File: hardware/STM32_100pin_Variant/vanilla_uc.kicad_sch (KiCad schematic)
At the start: 22 parts, among them J4 , U4 STM32L4S7VITx, U5 ATA6561-GAQW-N, Y2 Crystal_GND24

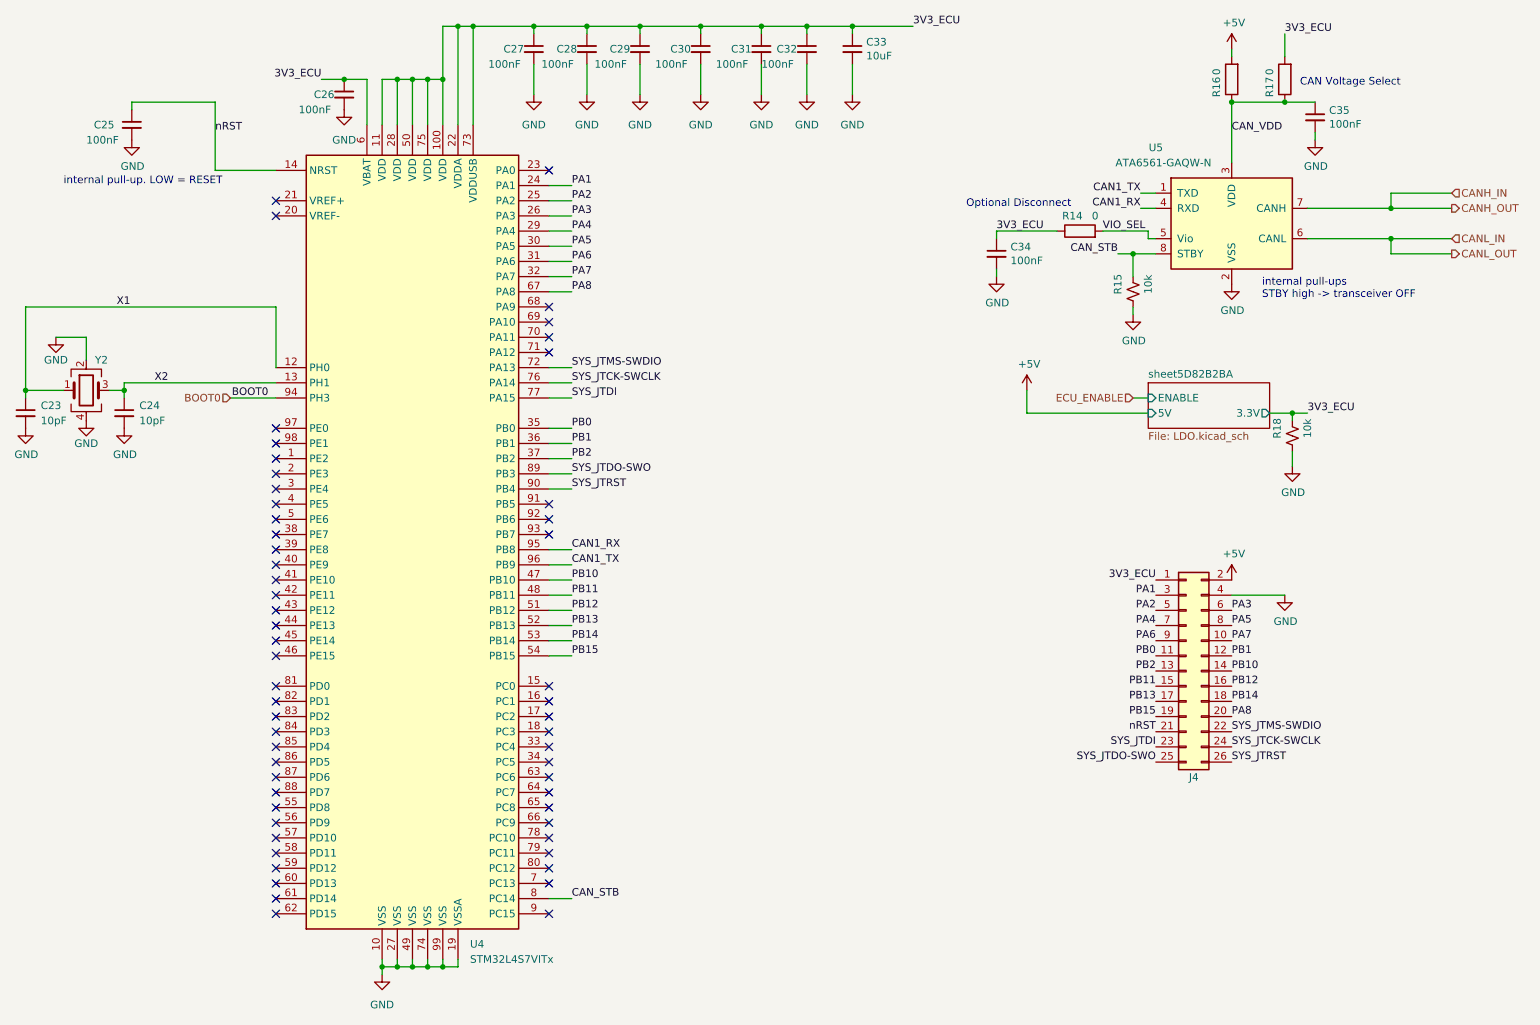
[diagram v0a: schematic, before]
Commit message: Schematic wiring fix, added part numbers
- Fixed missing connections between VREF+ and VDDA, VREF- and VSSA on all ECUs

- Added component part numbers for crystal and CAN trx to schematic
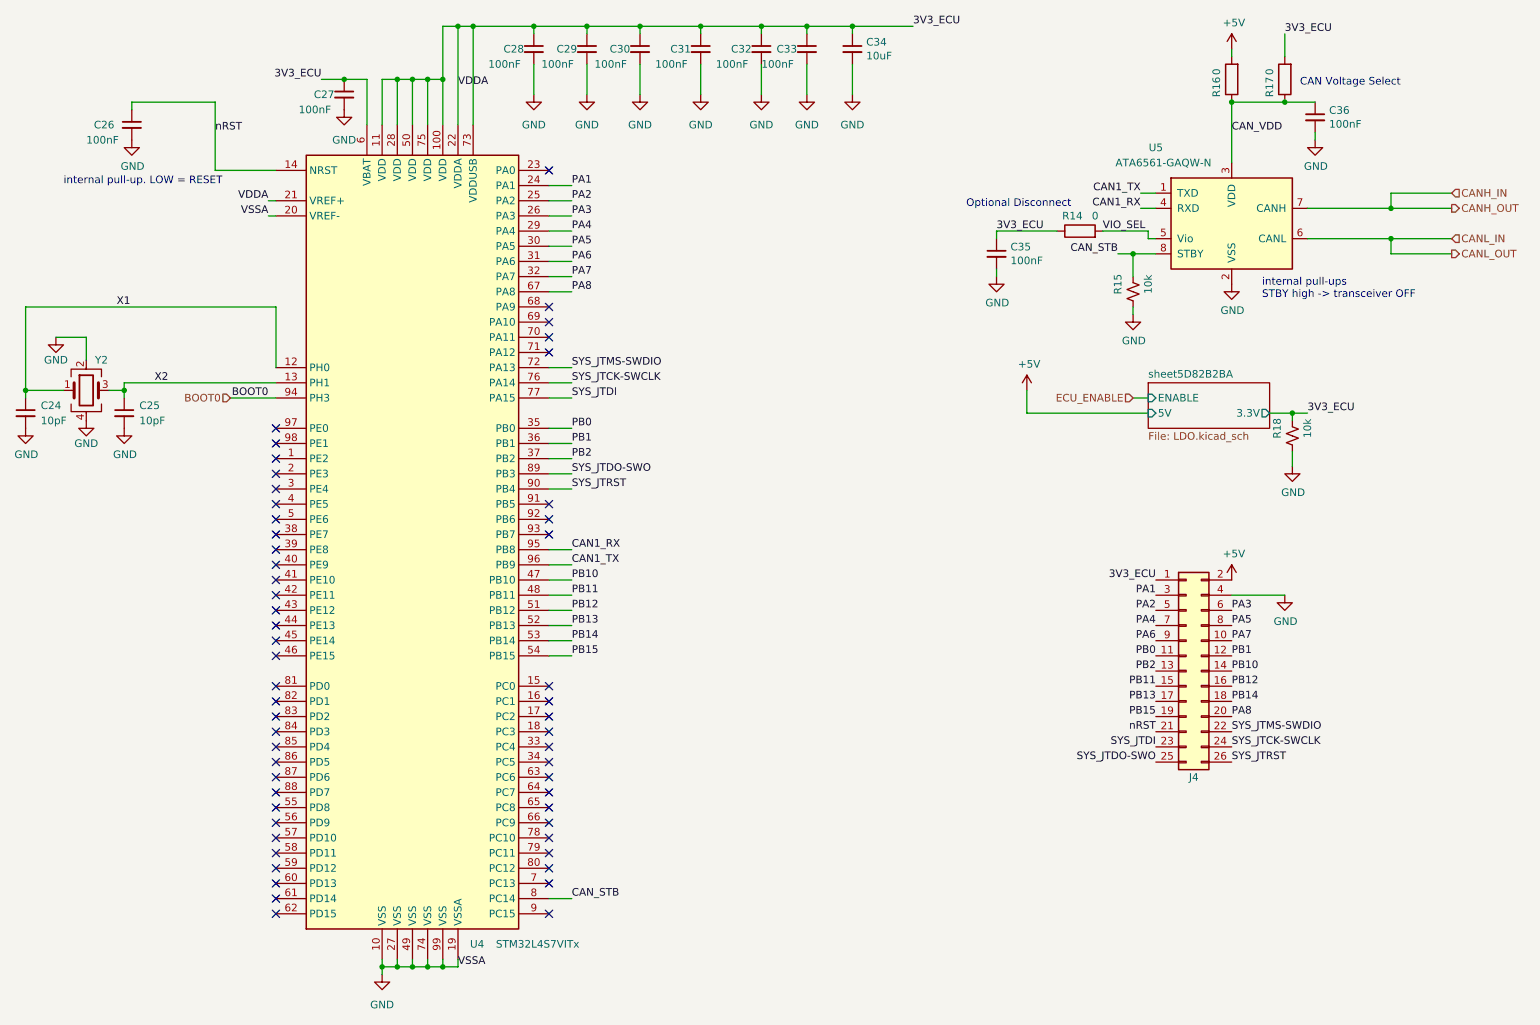
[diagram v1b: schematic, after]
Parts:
- U5: Part No. (none) -> TCAN1042HGVDRQ1
- Y2: Part No. (none) -> CX3225GB10000D0HEQCC
- renumbered C23 to C24, C24 to C25, C25 to C26, C26 to C27, C27 to C28, C28 to C29, C29 to C30, C30 to C31, C31 to C32, C32 to C33, C33 to C34, C34 to C35, C35 to C36
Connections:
- net 3V3_ECU: now also U4.21 (VREF+)
- net GND: now also U4.20 (VREF-)
- no-connect marks 57 -> 55

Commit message: Electrical Fix
- Fixed missing VREF+/- connections on ECUs

- Updated version number to V1.1

- Updated Gerbers

- Updated schematic PDF
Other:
- title: RAMN: Resistant Automotive Miniature Network V1.0 -> RAMN 100 Pin Variant
